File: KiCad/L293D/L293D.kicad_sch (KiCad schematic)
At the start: 12 parts, among them J10 Conn_01x03_Pin, J11 Conn_01x03_Pin, J12 Conn_01x02_Socket, J5 Conn_01x02_Pin, J6 Conn_01x02_Pin, J7 Conn_01x02_Pin, J8 Conn_01x02_Pin, J9 Conn_01x02_Socket, U1 L293D, U2 L293D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

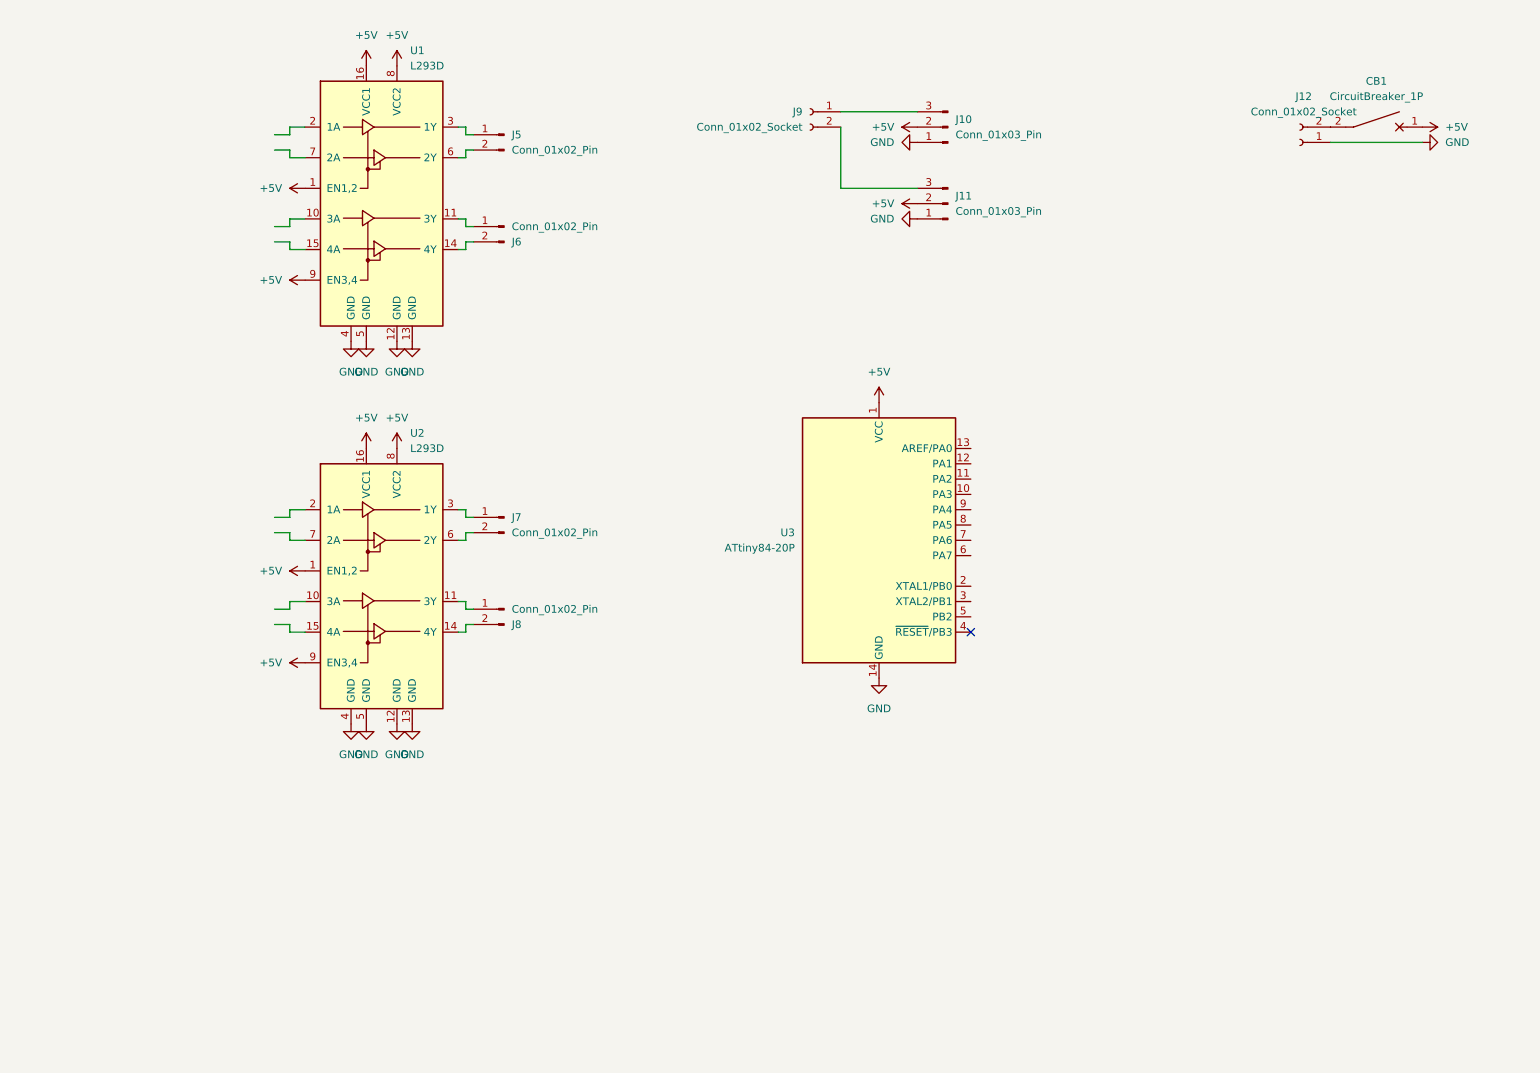
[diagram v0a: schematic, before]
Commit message: L293Dの基板をつくった
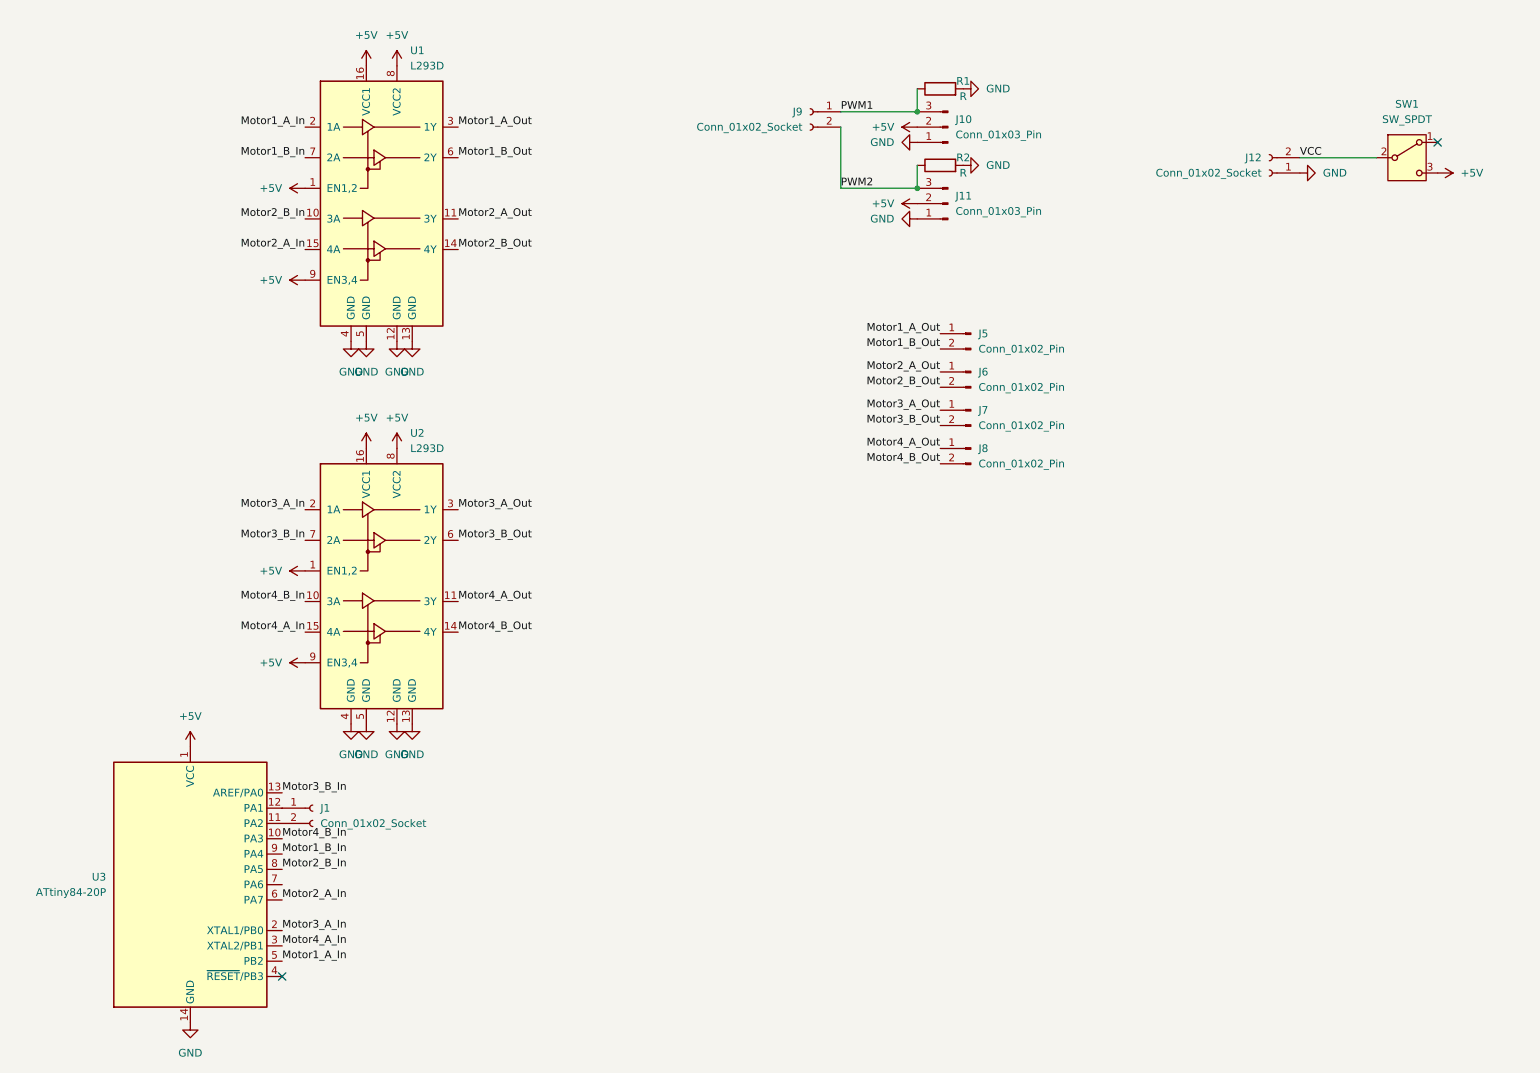
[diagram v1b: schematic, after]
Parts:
- removed CB1: CircuitBreaker_1P, symbol Device:CircuitBreaker_1P
- added J1: Conn_01x02_Socket, Connector_PinSocket_2.54mm:PinSocket_1x02_P2.54mm_Vertical, symbol Connector:Conn_01x02_Socket
- added R1, R2: R, Resistor_SMD:R_0603_1608Metric_Pad0.98x0.95mm_HandSolder, symbol Device:R
- added SW1: SW_SPDT, Connector_PinHeader_2.54mm:PinHeader_1x03_P2.54mm_Vertical, symbol Switch:SW_SPDT
- U3: footprint Package_DIP:DIP-14_W7.62mm -> Package_DIP:DIP-14_W7.62mm_Socket
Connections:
- net +5V: now also SW1.3 (C)
- net GND: now also R1.2, R2.2
- net PWM1: now reaches J10.3 (Pin_3), J9.1 (Pin_1)
- net PWM1: now also R1.1
- net PWM2: now reaches J11.3 (Pin_3), J9.2 (Pin_2)
- net PWM2: now also R2.1
- net Motor2_A_Out: now reaches J6.1 (Pin_1), U1.11 (3Y)
- net Motor2_B_Out: now reaches J6.2 (Pin_2), U1.14 (4Y)
- net Motor4_B_In: now reaches U3.10 (PA3)
- net Motor4_B_In: now also U2.10 (3A)
- net at U3.11 (PA2): now also J1.2 (Pin_2)
- net at U3.12 (PA1): now also J1.1 (Pin_1)
- net Motor3_B_In: now reaches U3.13 (AREF/PA0)
- net Motor3_B_In: now also U2.7 (2A)
- net Motor3_A_In: now reaches U3.2 (XTAL1/PB0)
- net Motor3_A_In: now also U2.2 (1A)
- net Motor4_A_In: now reaches U3.3 (XTAL2/PB1)
- net Motor4_A_In: now also U2.15 (4A)
- net Motor1_A_In: now reaches U3.5 (PB2)
- net Motor1_A_In: now also U1.2 (1A)
- net Motor2_A_In: now reaches U3.6 (PA7)
- net Motor2_A_In: now also U1.15 (4A)
- net Motor2_B_In: now reaches U3.8 (PA5)
- net Motor2_B_In: now also U1.10 (3A)
- net Motor1_B_In: now reaches U3.9 (PA4)
- net Motor1_B_In: now also U1.7 (2A)
- net Motor4_A_Out: now reaches J8.1 (Pin_1), U2.11 (3Y)
- net Motor4_B_Out: now reaches J8.2 (Pin_2), U2.14 (4Y)
- net Motor3_A_Out: now reaches J7.1 (Pin_1), U2.3 (1Y)
- net Motor3_B_Out: now reaches J7.2 (Pin_2), U2.6 (2Y)
- net VCC: now reaches J12.2 (Pin_2)
- net VCC: now also SW1.2 (B)
- net Motor1_A_Out: now reaches J5.1 (Pin_1), U1.3 (1Y)
- net Motor1_B_Out: now reaches J5.2 (Pin_2), U1.6 (2Y)
- no-connect marks 1 -> 2
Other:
- moved on the sheet: J12, J5, J6, J7, J8, U3

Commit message: L293D基板を更新 出力に直列抵抗を追加 パスコンを追加 リセット入力を追加
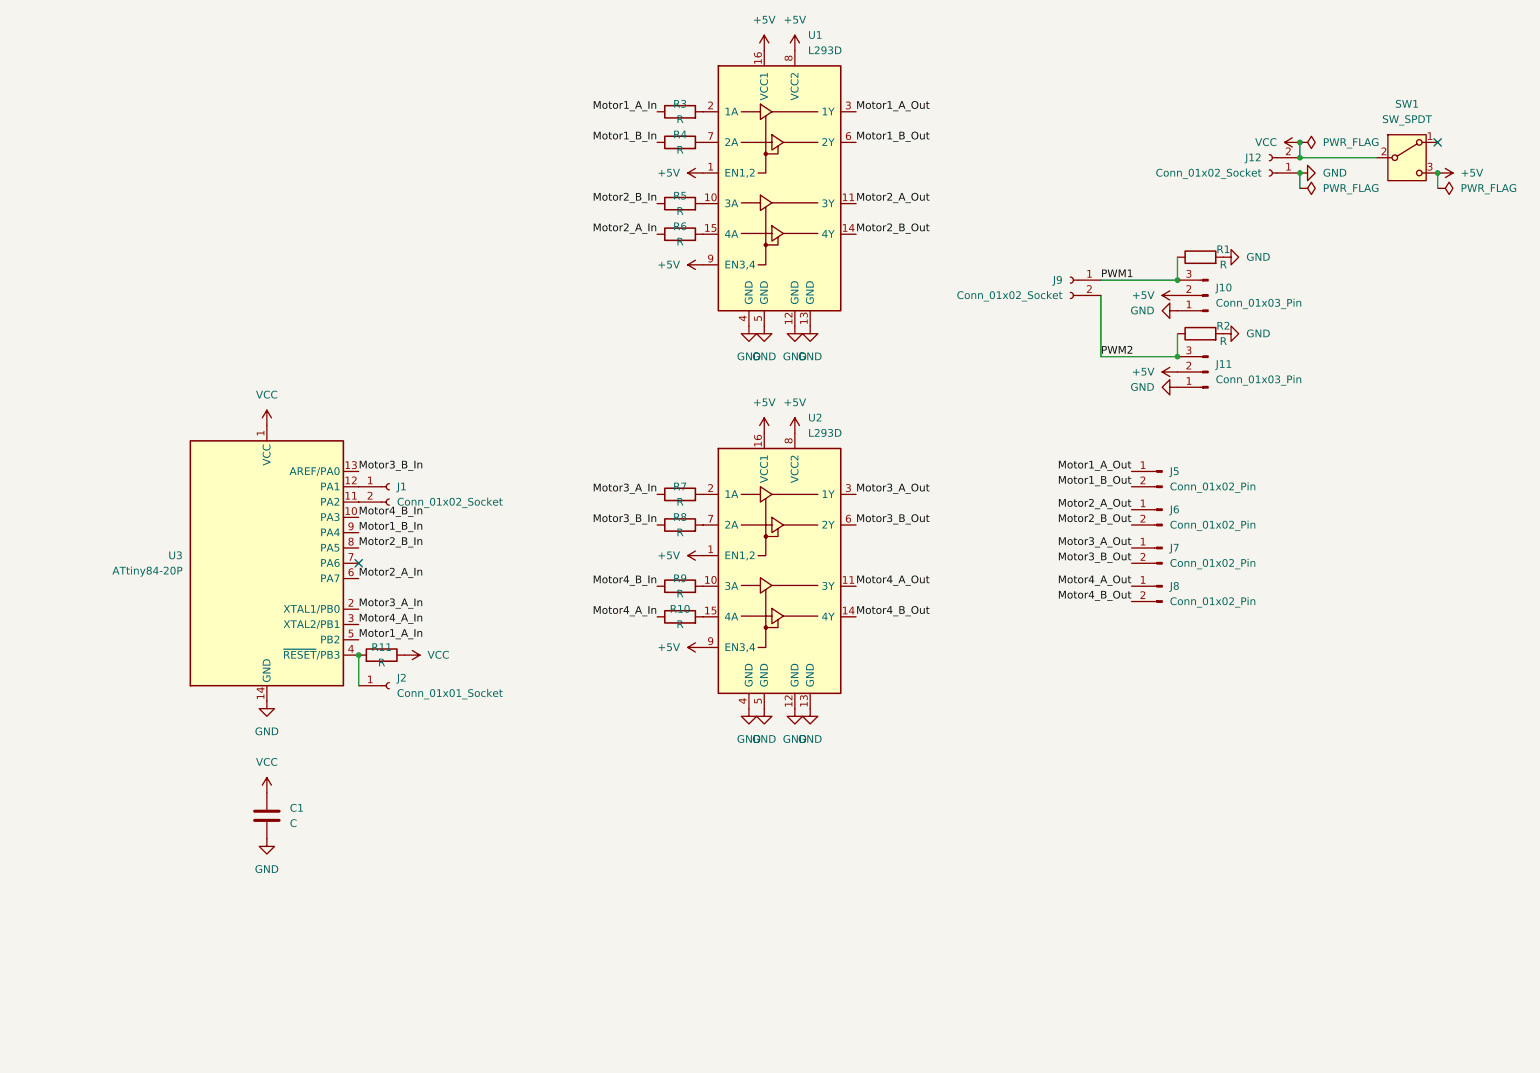
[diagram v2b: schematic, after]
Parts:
- added C1: C, Capacitor_SMD:C_0603_1608Metric_Pad1.08x0.95mm_HandSolder, symbol Device:C
- added J2: Conn_01x01_Socket, Connector_PinSocket_2.54mm:PinSocket_1x01_P2.54mm_Vertical, symbol Connector:Conn_01x01_Socket
- added R10, R11, R3, R4, R5, R6, R7, R8, R9: R, Resistor_SMD:R_0603_1608Metric_Pad0.98x0.95mm_HandSolder, symbol Device:R
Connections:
- net +5V: no longer U3.1 (VCC)
- net GND: now also C1.2
- net Motor1_A_In: now also R3.1; no longer U1.2 (1A)
- net Motor1_B_In: now also R4.1; no longer U1.7 (2A)
- net Motor2_A_In: now also R6.1; no longer U1.15 (4A)
- net Motor2_B_In: now also R5.1; no longer U1.10 (3A)
- net Motor3_A_In: now also R7.1; no longer U2.2 (1A)
- net Motor3_B_In: now also R8.1; no longer U2.7 (2A)
- net Motor4_A_In: now also R10.1; no longer U2.15 (4A)
- net Motor4_B_In: now also R9.1; no longer U2.10 (3A)
- net VCC: now also U3.1 (VCC), C1.1, R11.1
- net at U3.4 (~{RESET}/PB3): now also J2.1 (Pin_1), R11.2
- new net: R8.2, U2.7 (2A)
- new net: R5.2, U1.10 (3A)
- new net: R6.2, U1.15 (4A)
- new net: R9.2, U2.10 (3A)
- new net: R10.2, U2.15 (4A)
- new net: R7.2, U2.2 (1A)
- new net: R3.2, U1.2 (1A)
- new net: R4.2, U1.7 (2A)
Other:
- moved on the sheet: J1, J10, J11, J5, J6, J7, J8, J9, R1, R2, U1, U2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
